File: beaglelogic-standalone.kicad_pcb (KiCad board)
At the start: 6 copper layers, 100 x 60 mm, 252 parts, among them J1 USB_OTG, J2 CONN_02X02, J3 USB_A, J4 CONN_01X06, J5 SI-51009-F, J6 CONN_02X12, J7 CONN_02X16, J8 Barrel_Jack, M1 TEST_1P, M2 TEST_1P, M3 TEST_1P, M4 TEST_1P, Q1 BSS138, Q2 BSS138, SW1 SW_PUSH_SMALL_H, SW2 SW_PUSH_SMALL_H, U1 74LVC1G07, U10 MCP79410/TDFN, U11 SST26VF064B, U12 TPS73101, U13 SN74LVCH16T245, U14 DVIULC6-4SC6, U15 DVIULC6-4SC6, U16 DVIULC6-4SC6, U17 DVIULC6-4SC6, U18 74LV1T125, U19 EMMC_4G, U2 AP1117, U3 TPS2051C, U4 TPD4S012, U5 TPD4S012, U6 OSD3358-SM, U7 KSZ9031RNXCC, U8 74LVC2G241, U9 74LVC1G125, Y1 25MHz, Y2 24MHz, Y3 32.768kHz,CL=9pF

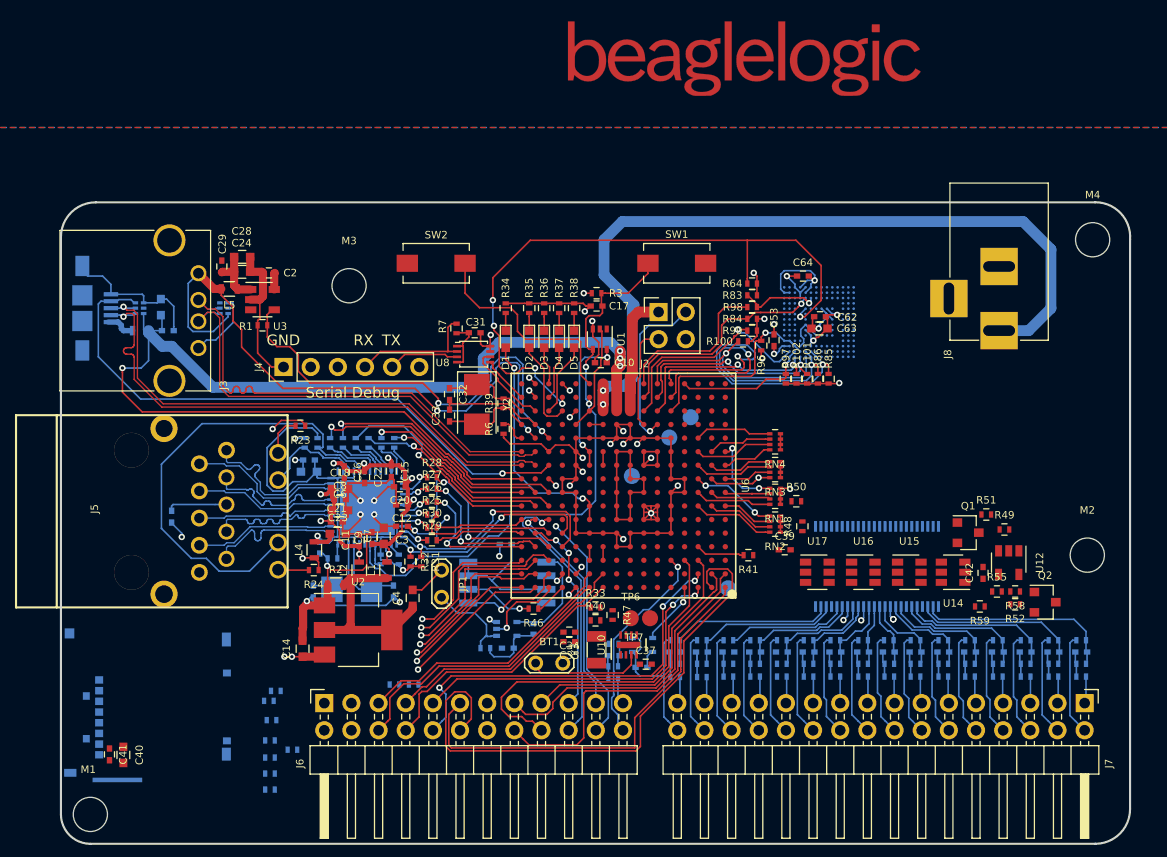
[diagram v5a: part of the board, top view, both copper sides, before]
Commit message: Almost 90% routed
Signed-off-by: Kumar Abhishek <abhishek@theembeddedkitchen.net>
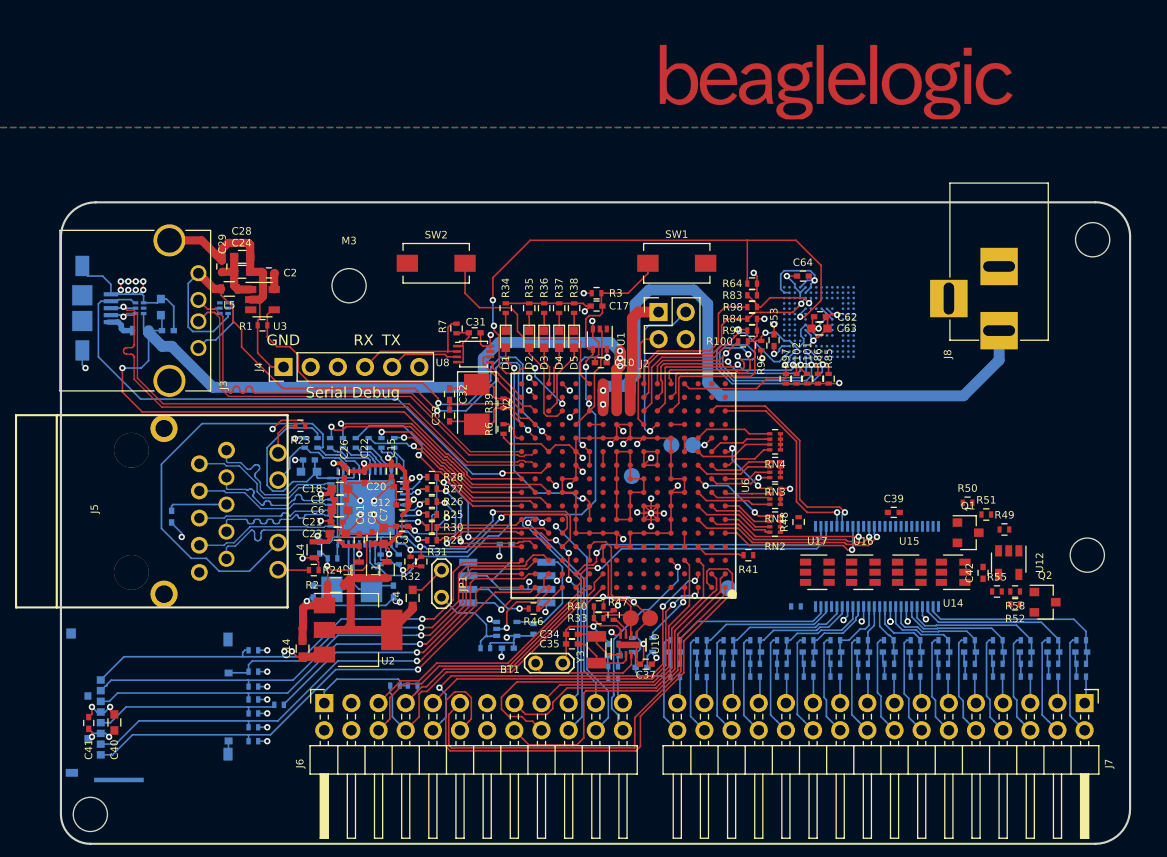
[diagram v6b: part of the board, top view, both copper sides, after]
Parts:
- R59: moved to B.Cu
- moved R59 17.2 mm to (169.8, 108.8), turned to 0 degrees
- moved R50 16.0 mm to (185.8, 99.1)
- moved C39 10.8 mm to (178.9, 100.0)
- moved LOGO1 8.88 mm to (173.5, 59.8)
- moved R63 4.95 mm to (119.0, 112.9)
- moved R54 4.79 mm to (119.0, 121.4)
- moved R57 4.60 mm to (119.0, 120.1)
- moved R60 4.41 mm to (119.0, 118.8)
- moved R56 4.38 mm to (121.4, 118.0), turned to 180 degrees
- moved R61 4.13 mm to (119.0, 117.5)
- moved R62 3.56 mm to (119.0, 116.3)
- moved C41 3.52 mm to (103.6, 119.7)
- moved C40 3.15 mm to (106.0, 119.7)
- moved R53 2.77 mm to (119.0, 114.9)
- moved TP4 2.61 mm to (160.1, 93.7)
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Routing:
- net GND: track 371.4 -> 411.8 mm, vias 30 -> 46
- net +3V3: track 73.9 -> 109.1 mm, vias 15 -> 33
- net /MMC0_DAT0: track 12.6 -> 46.8 mm
- net /MMC0_DAT1: track 14.1 -> 47.7 mm
- net /MMC0_DAT2: track 13.1 -> 46.5 mm
- net /MMC0_CMD: track 13.3 -> 46.3 mm
- net /MMC0_DAT3: track 15.2 -> 47.7 mm
- net /PRU1_IN14: track 0.96 -> 27.0 mm
- net /PRU1_IN15: track 0.87 -> 25.9 mm
- net /PRU1_IN12: track 0.00 -> 21.4 mm, vias 0 -> 1
- net /MMC0_CD: track 16.6 -> 36.8 mm
- net /PRU1_IN08: track 0.00 -> 19.2 mm, vias 0 -> 1
- net /PRU1_IN13: track 0.00 -> 19.0 mm, vias 0 -> 1
- net Net-(R56-Pad2): track 0.00 -> 17.8 mm
- net I2C0_SDA: track 1.27 -> 19.1 mm, vias 0 -> 2
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- added copper zone on In2.Cu, net +3V3
- added copper zone on In3.Cu, net GND
- removed copper zone on In3.Cu, net +3V3
- removed copper zone on In2.Cu, net GND

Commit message: Finish routing
Signed-off-by: Kumar Abhishek <abhishek@theembeddedkitchen.net>
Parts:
- added C65: 0.1uF, Capacitors_SMD:C_0402, B.Cu at (180.2, 99.3)
- added C66: 0.1uF, Capacitors_SMD:C_0402, F.Cu at (175.2, 109.4)
- C39, Q1, Q2, R48, R49, R50, R51, R52, R55, R58, U12: moved to B.Cu
- moved LOGO1 36.9 mm to (188.2, 93.7)
- moved R48 13.1 mm to (183.0, 99.7)
- moved TP2 12.6 mm to (153.7, 99.1)
- moved R51 10.7 mm to (178.0, 95.4), turned to 270 degrees
- moved R49 8.80 mm to (183.0, 95.4), turned to 90 degrees
- moved Q2 8.75 mm to (186.5, 102.6), turned to 270 degrees
- moved C42 8.70 mm to (179.4, 109.4), turned to 0 degrees
- moved Q1 7.89 mm to (180.5, 96.1), turned to 270 degrees
- moved R58 4.32 mm to (188.9, 103.3), turned to 270 degrees
- moved R52 4.05 mm to (188.6, 104.9), turned to 0 degrees
- moved C39 3.26 mm to (175.7, 99.4), turned to 180 degrees
- moved U12 1.98 mm to (191.5, 104.0), turned to 180 degrees
- moved U17 1.35 mm to (170.5, 106.1)
- moved R55 1.30 mm to (188.6, 106.1), turned to 180 degrees
- moved TP3 1.14 mm to (155.1, 95.7)
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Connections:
- U10 pad 9: GND -> (no net)
- U14 pad 1: /DIN00 -> /DIN03
- U14 pad 4: /DIN03 -> /DIN00
- U15 pad 1: /DIN04 -> /DIN07
- U15 pad 4: /DIN07 -> /DIN04
- U16 pad 1: /DIN08 -> /DIN11
- U16 pad 4: /DIN11 -> /DIN08
- U17 pad 1: /DIN12 -> /DIN15
- U17 pad 4: /DIN15 -> /DIN12
- U19 pad A1: /EMMC_DAT3 -> (no net)
- U19 pad A2: /EMMC_DAT4 -> (no net)
- U19 pad A6: /EMMC_DAT6 -> (no net)
- U19 pad A7: /EMMC_DAT7 -> (no net)
- U19 pad N1: GND -> (no net)
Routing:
- net SYS_5V: track 7.79 -> 260.1 mm, vias 1 -> 2
- net GND: track 411.8 -> 510.6 mm, vias 46 -> 54
- net Net-(C42-Pad2): track 2.86 -> 56.6 mm, vias 2 -> 3
- net /GPIO_VSEL: track 0.80 -> 52.6 mm, vias 1 -> 2
- net /GPIO_OE: track 0.87 -> 38.8 mm, vias 1 -> 2
- net Net-(R59-Pad2): track 0.00 -> 30.0 mm
- net +3V3: track 109.1 -> 138.0 mm, vias 33 -> 36
- net Net-(Q1-Pad3): track 0.00 -> 20.8 mm, vias 0 -> 2
- net /PRU1_IN00: track 7.82 -> 28.2 mm, vias 0 -> 3
- net /PRU1_IN01: track 6.24 -> 25.4 mm, vias 0 -> 3
- net /PRU1_IN02: track 4.76 -> 23.5 mm, vias 0 -> 3
- net /PRU1_IN03: track 7.16 -> 25.6 mm, vias 0 -> 3
- net /PRU1_IN04: track 5.69 -> 23.8 mm, vias 0 -> 3
- net /PRU1_IN05: track 4.28 -> 21.7 mm, vias 0 -> 3
- net /PRU1_IN07: track 5.85 -> 21.1 mm
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- removed copper zone on In3.Cu, net GND
- removed copper zone on In4.Cu, net GND
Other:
- copper layers 6 -> 4

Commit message: Shrink and add logo
Signed-off-by: Kumar Abhishek <abhishek@theembeddedkitchen.net>
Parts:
- moved LOGO1 3.10 mm to (185.1, 93.8)
- moved M2 0.61 mm to (197.6, 103.9)
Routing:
- added copper zone on F.Cu, net VDDSHV
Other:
- board text added: "BeagleLogic Standalone REV A Copyright © 2017 Kumar Abhishek"
